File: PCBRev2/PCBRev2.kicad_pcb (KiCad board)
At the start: 2 copper layers, 213.4 x 128.3 mm, 60 parts, among them J1 54-00164, J2 Conn_02x10_Odd_Even, J4 Keypad, J6 Conn_02x30_Odd_Even, J7 512964594, Q1 2N4401, SW1 SW_Push, SW2 SW_Push, SW3 SW_Push, U1 NUCLEO-G0B1RE, U10 AL5809-20QP1-7, U11 MCP6002-I_P, U2 LM7805_TO220, U3 TLV1117-33, U4 LP-MSPM0G3507, U5 COM-09032, U6 DRV8833PWP, U7 SN74AHC14N, U8 BH1750FVI-TR, U9 WST-1205S

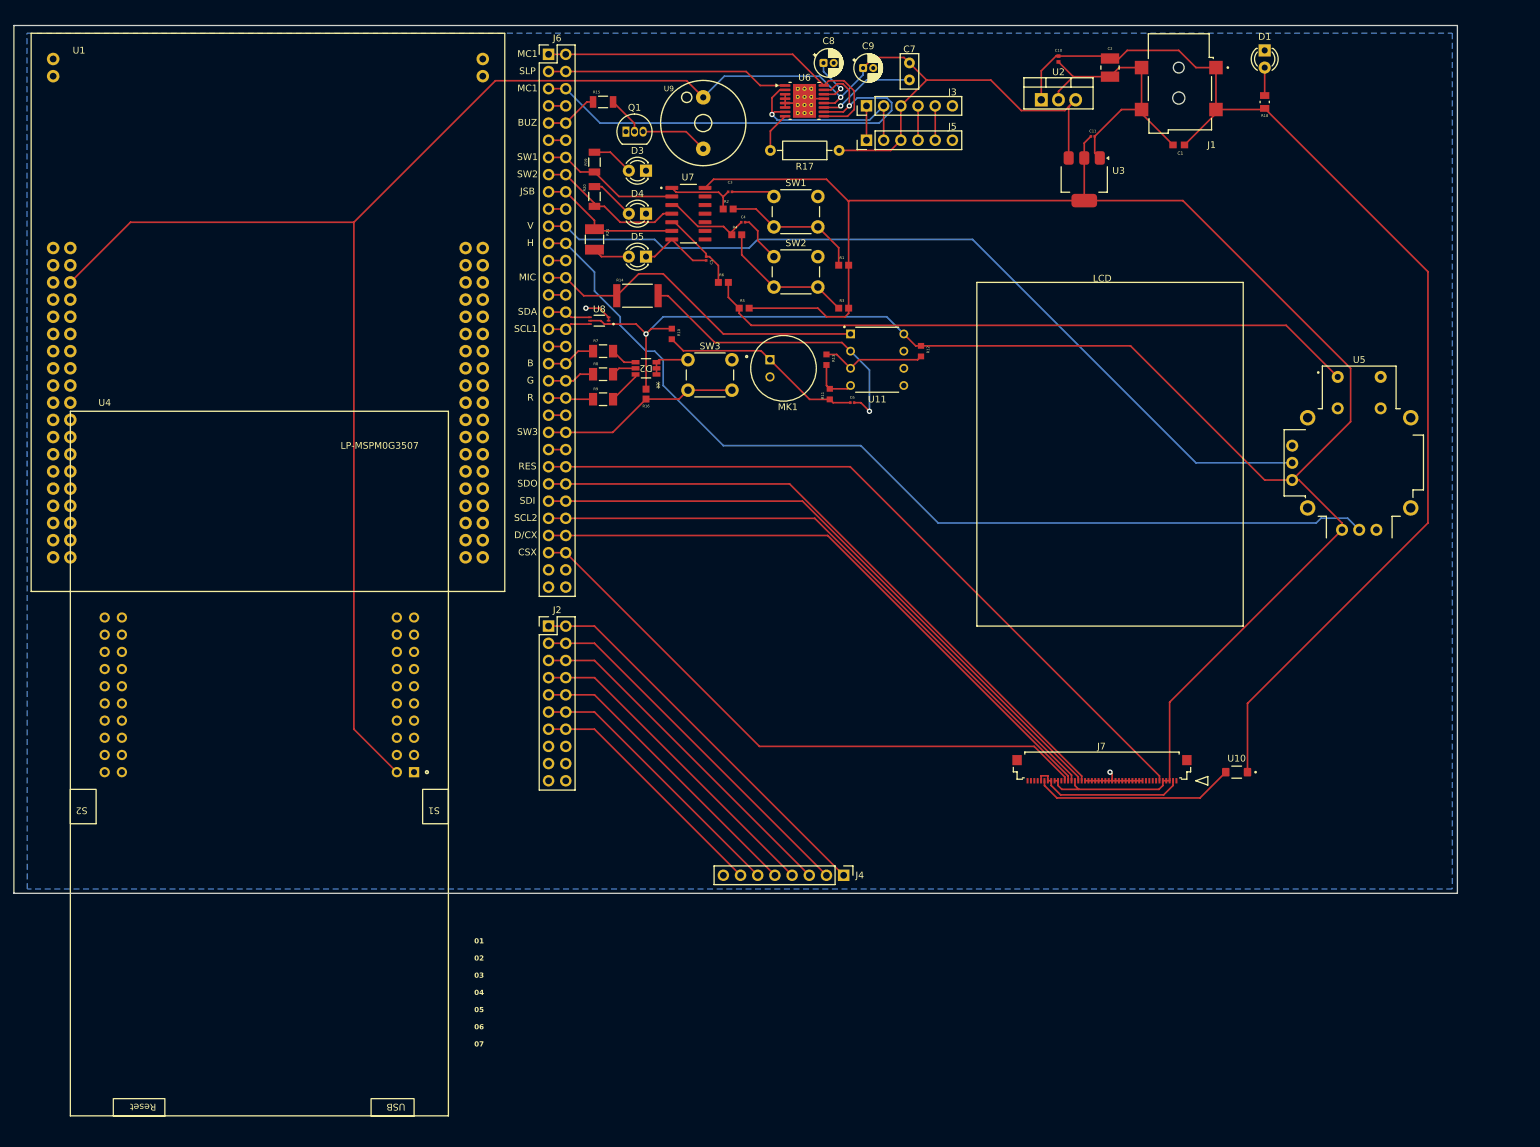
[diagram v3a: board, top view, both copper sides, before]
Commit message: Updated silkscreen
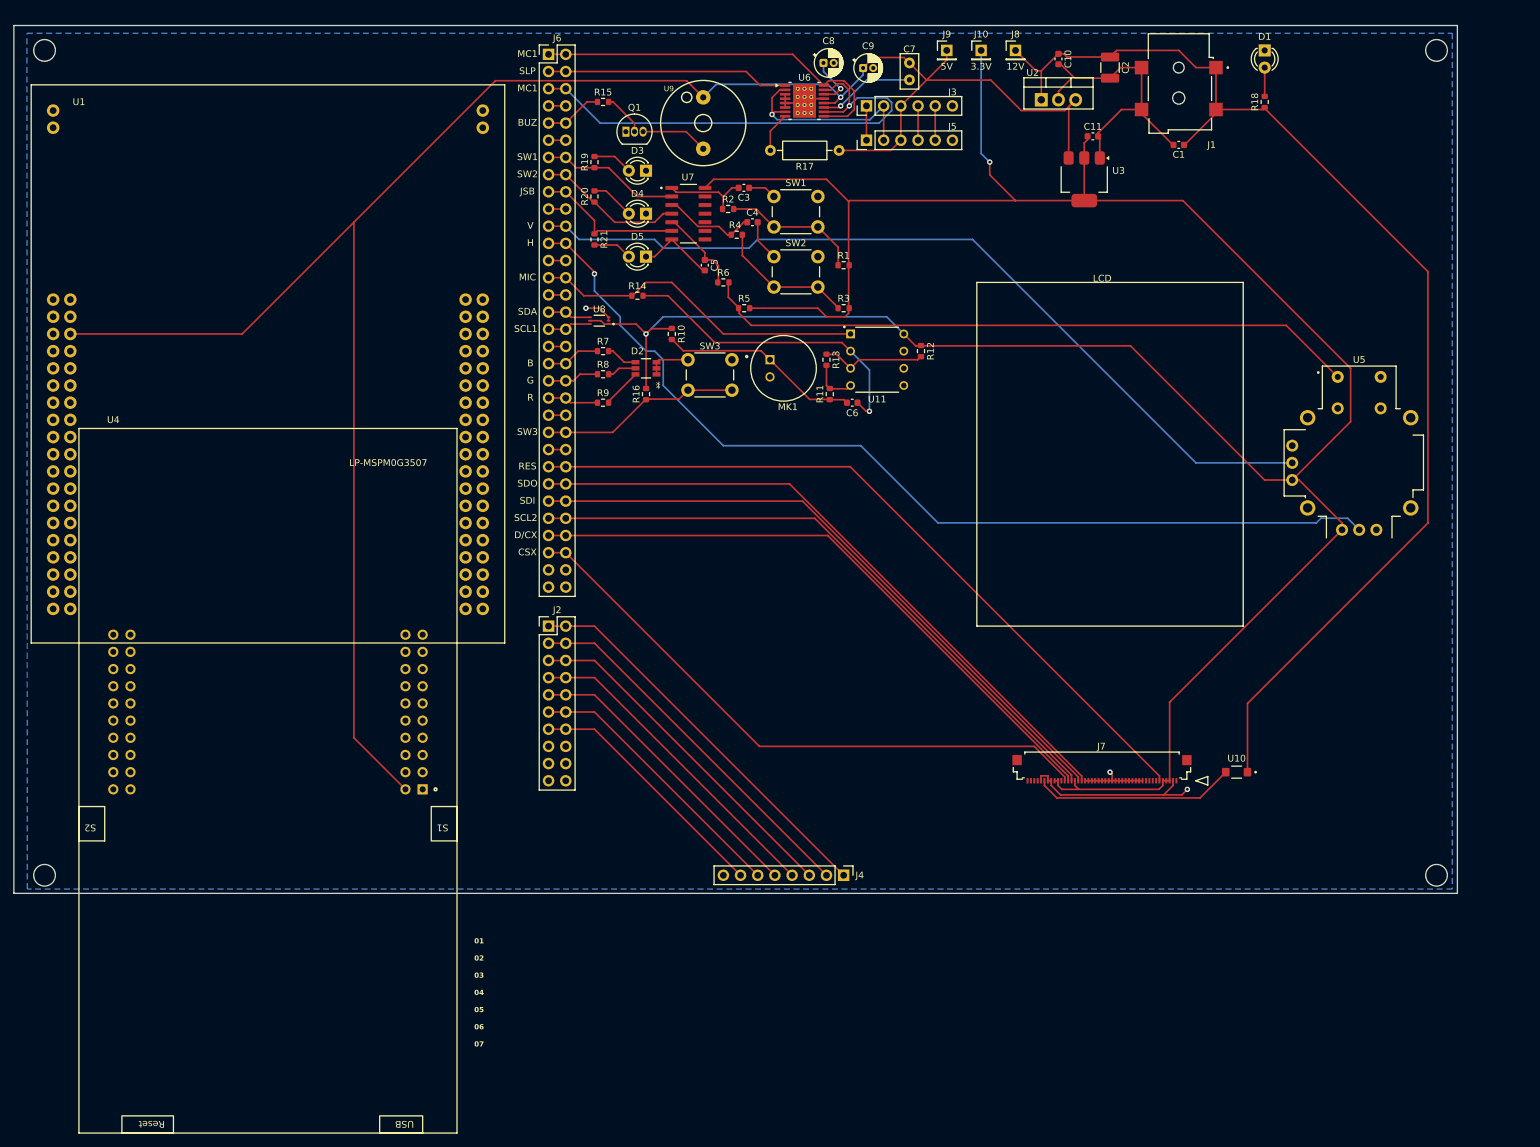
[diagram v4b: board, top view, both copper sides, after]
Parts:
- added J10: 3.3V, Connector_PinHeader_2.54mm:PinHeader_1x01_P2.54mm_Vertical, F.Cu at (153.7, 15.2)
- added J8: 12V, Connector_PinHeader_2.54mm:PinHeader_1x01_P2.54mm_Vertical, F.Cu at (158.8, 15.2)
- added J9: 5V, Connector_PinHeader_2.54mm:PinHeader_1x01_P2.54mm_Vertical, F.Cu at (148.6, 15.2)
- added REF**: MountingHole_3.2mm_M3, MountingHole:MountingHole_3.2mm_M3, F.Cu at (15.2, 15.2)
- added REF**: MountingHole_3.2mm_M3, MountingHole:MountingHole_3.2mm_M3, F.Cu at (221.0, 15.2)
- added REF**: MountingHole_3.2mm_M3, MountingHole:MountingHole_3.2mm_M3, F.Cu at (15.2, 137.2)
- added REF**: MountingHole_3.2mm_M3, MountingHole:MountingHole_3.2mm_M3, F.Cu at (221.0, 137.2)
- C1: footprint C01UF.step:CAPC1608X90 -> Capacitor_SMD:C_0603_1608Metric
- C10: footprint GRM155R71C224KA12D022uf.step:CAPC1005X55N -> Capacitor_SMD:C_0603_1608Metric
- C11, C6: footprint CL03A105KP3NSNC1uf.step:CAPC0603X35N -> Capacitor_SMD:C_0603_1608Metric
- C2: footprint GRM32EC81C476KE15L.step:CAPC3225X270N -> Capacitor_SMD:C_1210_3225Metric_Pad1.33x2.70mm_HandSolder
- C3, C4, C5: footprint GRM033R60J474KE90D.step:CAPC0603X33N -> Capacitor_SMD:C_0603_1608Metric
- R1, R16, R2, R3, R4, R5, R6: footprint RC0603FR_0710KL.step:RESC1607X60N -> Resistor_SMD:R_0603_1608Metric
- R10, R11, R12, R13: footprint CRGCQ0603F2K2.step:RESC1608X55N -> Resistor_SMD:R_0603_1608Metric
- R14: footprint CRGP2512F68K.step:RESC6332X65N -> Resistor_SMD:R_0603_1608Metric
- R15: footprint RC1206JR_07620RL.step:RESC3116X65N -> Resistor_SMD:R_0603_1608Metric
- R18: footprint RMCF0805JT510R510.step:RESC2012X65N -> Resistor_SMD:R_0603_1608Metric
- R19, R20: footprint CRGCQ1206F68R.step:RESC3115X65N -> Resistor_SMD:R_0603_1608Metric
- R21: footprint CRCW1210330RFKEAHP.step:RESC3225X70N -> Resistor_SMD:R_0603_1608Metric
- R7, R8: value 1kR -> 300; footprint RNCP1206FTD1K00.step:RESC3216X90N -> Resistor_SMD:R_0603_1608Metric
- R9: value 1kR -> 750; footprint RNCP1206FTD1K00.step:RESC3216X90N -> Resistor_SMD:R_0603_1608Metric
- U7: value SN74AHC14N -> SN74AHCT14QDRG4Q1
- moved U1 7.62 mm to (48.3, 61.6)
- moved U4 2.84 mm to (48.3, 121.9)
- moved C3 2.12 mm to (118.6, 35.6)
- moved C4 1.38 mm to (119.9, 40.6)
- moved C5 1.01 mm to (112.8, 47.0)
- moved R9 0.51 mm to (97.8, 67.3)
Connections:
- net +3.3V renamed Net-(U1B-3V3-PadCN6_2)
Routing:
- net VDD: track 376.6 -> 400.7 mm, vias 1 -> 2
- net +5V: track 287.5 -> 298.3 mm
- net +12V: track 172.5 -> 178.4 mm
- net Net-(U7-1A): track 11.0 -> 12.8 mm
- net Net-(U11-VINA-): track 44.7 -> 46.4 mm
- net Net-(D2-Pad6): track 5.05 -> 6.13 mm
- net MicOut: track 50.8 -> 49.7 mm
- net R: track 6.65 -> 7.52 mm
- net Net-(U7-3A): track 12.3 -> 13.1 mm
- net JSB: track 21.4 -> 22.1 mm
- net Net-(Q1-G): track 5.70 -> 6.36 mm
- net BuzzerGPIO: track 7.87 -> 8.52 mm
- net Net-(D2-Pad5): track 3.68 -> 4.34 mm
- net Net-(D2-Pad4): track 4.00 -> 4.65 mm
- net G: track 6.98 -> 7.64 mm
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
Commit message: Updated PCB
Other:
- board text added: "1"
- board text added: "2"
- board text added: "3"
- board text added: "4"
- board text added: "5"
- board text added: "6"
- board text added: "7"
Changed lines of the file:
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@@
 		(layer "Edge.Cuts")
+	)
+	(gr_text "4"
+		(at 87.63 107.95 0)
+		(layer "F.SilkS")
+		(effects
+			(font
+				(size 1 1)
+				(thickness 0.15)
+			)
+		)
 	)
 	(gr_text "07"
@@
 		)
 	)
+	(gr_text "2"
+		(at 87.63 102.87 0)
+		(layer "F.SilkS")
+		(effects
+			(font
+				(size 1 1)
+				(thickness 0.15)
+			)
+		)
+	)
 	(gr_text "01"
 		(at 78.74 147.32 0)
@@
 		)
 	)
+	(gr_text "1"
+		(at 87.63 100.33 0)
+		(layer "F.SilkS")
+		(effects
+			(font
+				(size 1 1)
+				(thickness 0.15)
+			)
+		)
+	)
 	(gr_text "04"
 		(at 78.74 154.94 0)
@@
 		)
 	)
+	(gr_text "3"
+		(at 87.63 105.41 0)
+		(layer "F.SilkS")
+		(effects
+			(font
+				(size 1 1)
+				(thickness 0.15)
+			)
+		)
+	)
 	(gr_text "  H"
 		(at 86.614 43.688 0)
@@
 		(layer "F.SilkS")
 		(effects
+			(font
+				(size 1 1)
+				(thickness 0.15)
+			)
+		)
+	)
+	(gr_text "7"
+		(at 87.63 115.57 0)
+		(layer "F.SilkS")
+		(effects
+			(font
+				(size 1 1)
+				(thickness 0.15)
+			)
+		)
+	)
+	(gr_text "5"
+		(at 87.63 110.49 0)
+		(layer "F.SilkS")
+		(effects
+			(font
+				(size 1 1)
+				(thickness 0.15)
+			)
+		)
+	)
+	(gr_text "6"
+		(at 87.63 113.03 0)
+		(layer "F.SilkS")
+		(effects
